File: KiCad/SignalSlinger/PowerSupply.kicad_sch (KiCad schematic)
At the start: 44 parts, among them J201 Barrel_Jack_Switch, J203 External Fan Power, J204 Controlled Power, U201 LP2985-3.3, U202 LP2985-3.3, U203 TPS63060, U204 TPS22810DBVT, U205 uA7805

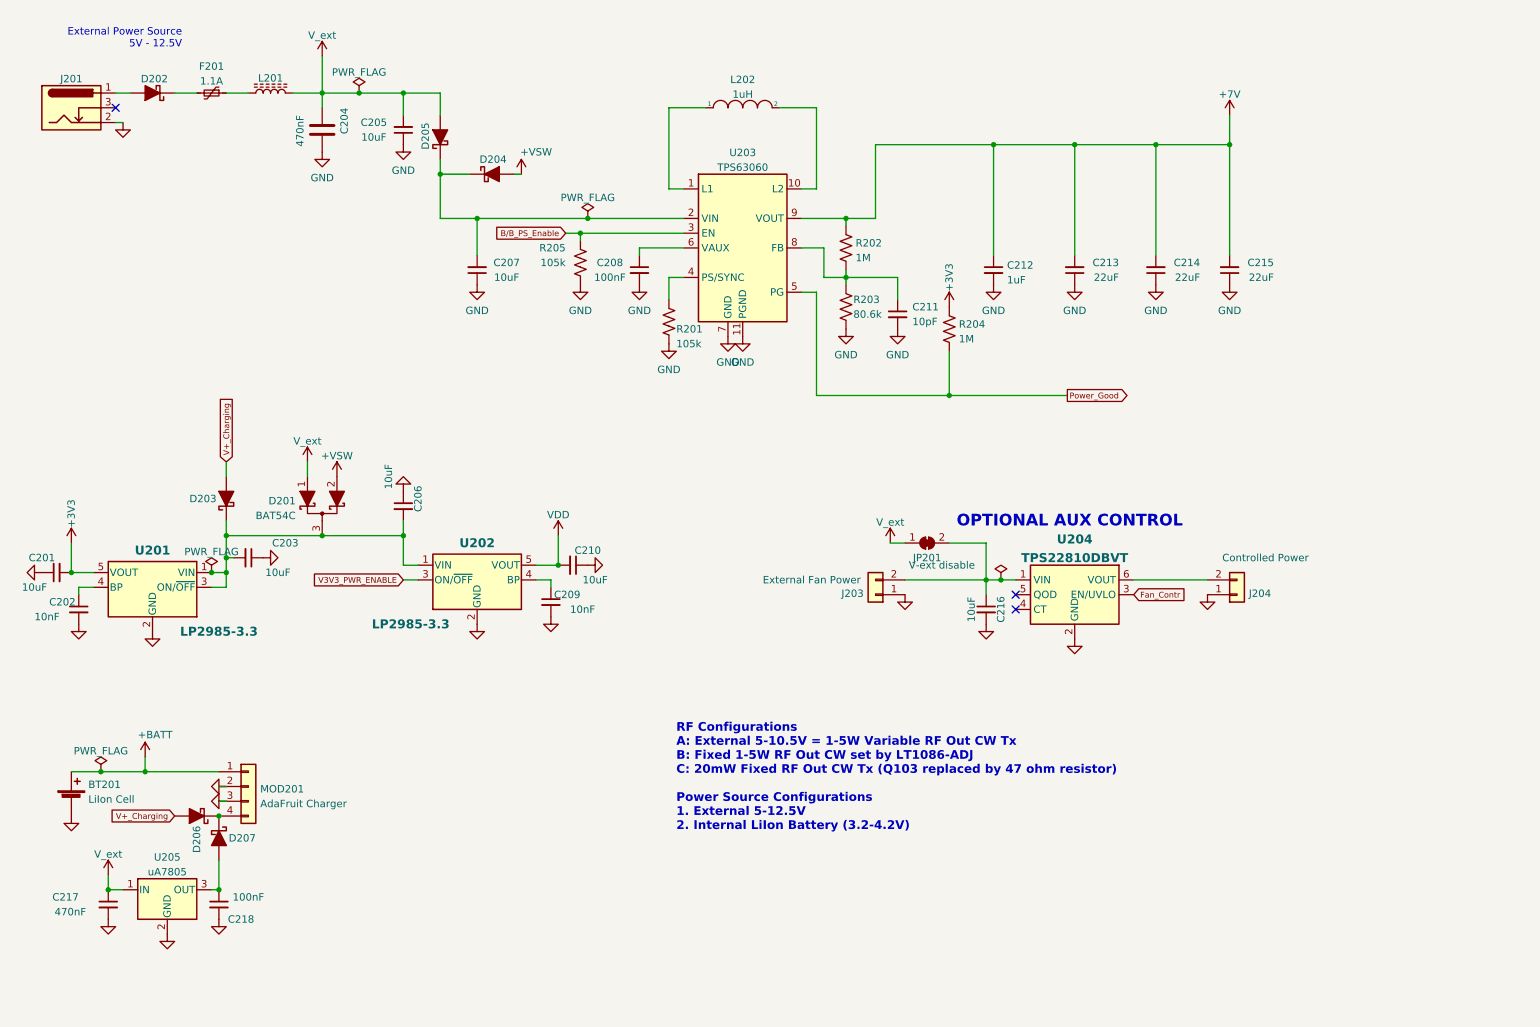
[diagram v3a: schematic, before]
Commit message: Added voltage divider
Now supports monitoring external battery voltage.
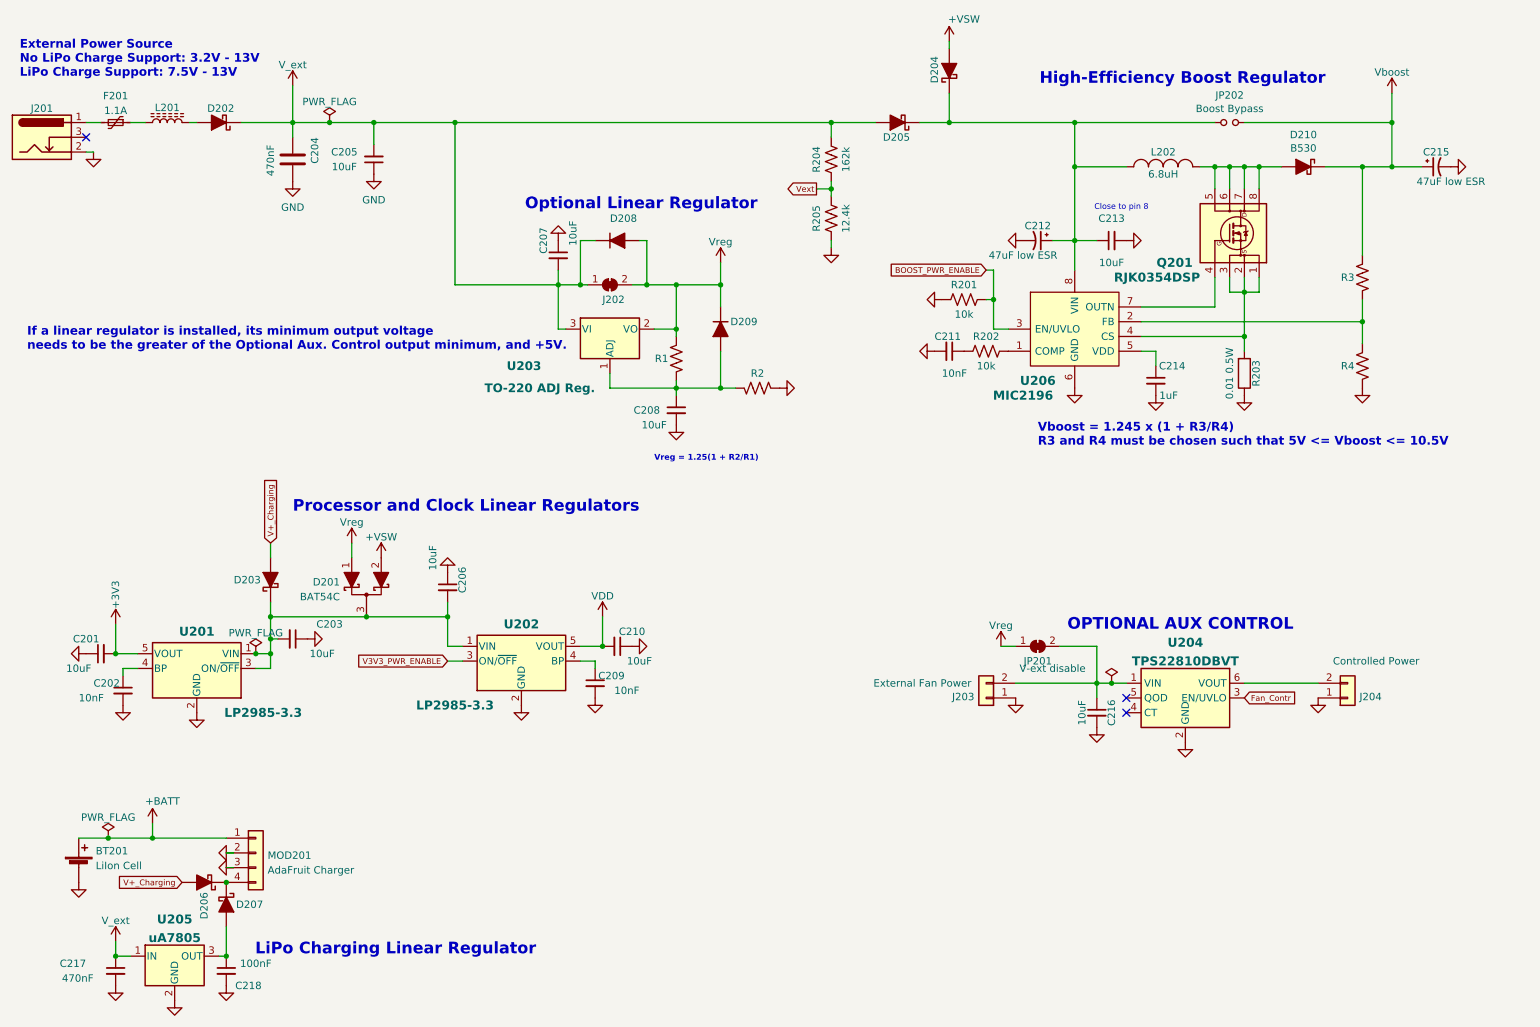
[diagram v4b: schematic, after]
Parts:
- removed C212: 1uF, Capacitor_SMD:C_0805_2012Metric, symbol Device:C_Small
- removed C215: 22uF, Capacitor_SMD:C_0805_2012Metric, symbol Device:C_Small
- removed L202: 1uH, Inductor_SMD:L_Bourns_SRN5040TA, symbol pspice:INDUCTOR
- removed R203: 80.6k, Resistor_SMD:R_0805_2012Metric, symbol Device:R_Small_US
- removed U203: TPS63060, Package_SON:Texas_S-PWSON-N10_ThermalVias, symbol Regulator_Switching:TPS63060
- added C212, C215: 47uF low ESR, Capacitors:C_2917, symbol Device:CP1_Small-Device
- added D208, D209: 1N4001, Diode_SMD:D_SOD-123F, symbol Diode:1N914WT
- added D210: B530, Diode_SMD:D_SMC, symbol FlexFox80-rescue:D_Schottky_ALT-Device
- added J202: SolderJumper_2_Bridged, Jumper:SolderJumper-2_P1.3mm_Bridged_RoundedPad1.0x1.5mm, symbol Jumper:SolderJumper_2_Bridged
- added JP202: Boost Bypass, Jumper:SolderJumper-2_P1.3mm_Open_RoundedPad1.0x1.5mm, symbol FlexFox80-rescue:Jumper_NO_Small-Device
- added L202: 6.8uH, Inductors:CDR7D28MN, symbol FlexFox80-rescue:INDUCTOR_SMALL-ARDF-2-Band-MiniTx-rescue
- added Q201: RJK0354DSP, Package_SO:SOIC-8_3.9x4.9mm_P1.27mm, symbol FlexFox80-rescue:SI4884BDY-Transistor_FET
- added R1, R2, R3, R4: TBD, Resistor_THT:R_Axial_DIN0204_L3.6mm_D1.6mm_P2.54mm_Vertical, symbol Device:R_Small_US
- added R203: 0.01 0.5W, Resistor_SMD:R_0805_2012Metric, symbol Device:R
- added U203: TO-220 ADJ Reg., Package_TO_SOT_THT:TO-220-3_Horizontal_TabDown, symbol Regulator_Linear:LT1086-ADJ
- added U206: MIC2196, Package_SO:SOIC-8_3.9x4.9mm_P1.27mm, symbol FlexFox80-rescue:MIC2196-Power_Management
- C208: value 100nF -> 10uF; Digi-Key Part No. 1276-1099-1-ND -> 445-14418-1-ND; LCSC Part Number C29926 -> C3843628; Link https://www.digikey.com/short/q2f22qnq -> https://www.digikey.com/short/p8qdn4mp; Manufacturer Samsung Electro-Mechanics -> TDK Corporation; Manufacturer PN CL21B104KACNNNC -> C2012X5R1V106K125AC
- C211: value 10pF -> 10nF; Digi-Key Part No. 478-KGM21BCG1H100JTCT-ND -> 399-C0805C103J5GEC7800CT-ND; LCSC Part Number C157608 -> C3887673; Link https://www.digikey.com/en/products/detail/kyocera-avx/KGM2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 -> https://www.digikey.com/short/qd893213; Manufacturer KYOCERA AVX -> KEMET; Manufacturer PN KGM21BCG1H100JT -> C0805C103J5GEC7800
- C213: value 22uF -> 10uF; Digi-Key Part No. 1276-6780-1-ND -> 445-14418-1-ND; LCSC Part Number (none) -> C3843628; Link (none) -> https://www.digikey.com/short/p8qdn4mp; Manufacturer Samsung Electro-Mechanics -> TDK Corporation; Manufacturer PN CL21A226MOCLRNC -> C2012X5R1V106K125AC
- C214: value 22uF -> 1uF; Digi-Key Part No. 1276-6780-1-ND -> 311-1365-1-ND; LCSC Part Number (none) -> C344171; Link (none) -> <a href="https://www.digikey.com/products/en?keywords=311-1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; Manufacturer Samsung Electro-Mechanics -> Yageo; Manufacturer PN CL21A226MOCLRNC -> CC0805KKX7R7BB105
- R201: value 105k -> 10k; footprint Resistor_SMD:R_0805_2012Metric -> Capacitor_SMD:C_0805_2012Metric; Digi-Key Part No. 311-105KCRCT-ND -> RNCP0805FTD10K0CT-ND; LCSC Part Number C273877 -> C2441435; Link https://www.digikey.com/en/products/detail/yageo/RC0805FR-0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 -> https://www.digikey.com/en/products/detail/stackpole-electr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; Manufacturer YAGEO -> Stackpole Electronics Inc; Manufacturer PN RC0805FR-07105KL -> RNCP0805FTD10K0
- R202: value 1M -> 10k; footprint Resistor_SMD:R_0805_2012Metric -> Capacitor_SMD:C_0805_2012Metric; Digi-Key Part No. 13-RC0805FR-131MLCT-ND -> RNCP0805FTD10K0CT-ND; LCSC Part Number C4198744 -> C2441435; Link https://www.digikey.com/en/products/detail/yageo/RC0805FR-1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 -> https://www.digikey.com/en/products/detail/stackpole-electr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; Manufacturer YAGEO -> Stackpole Electronics Inc; Manufacturer PN RC0805FR-131ML -> RNCP0805FTD10K0
- R204: value 1M -> 162k; Digi-Key Part No. 13-RC0805FR-131MLCT-ND -> 311-162KCRCT-ND; LCSC Part Number C4198744 -> C273888; Link https://www.digikey.com/en/products/detail/yageo/RC0805FR-1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 -> https://www.digikey.com/en/products/detail/yageo/RC0805FR-0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; Manufacturer PN RC0805FR-131ML -> RC0805FR-07162KL
- R205: value 105k -> 12.4k; Digi-Key Part No. 311-105KCRCT-ND -> 311-12.4KCRCT-ND; LCSC Part Number C273877 -> C137595; Link https://www.digikey.com/en/products/detail/yageo/RC0805FR-07105KL/727548 -> https://www.digikey.com/en/products/detail/yageo/RC0805FR-0712K4L/727572; Manufacturer PN RC0805FR-07105KL -> RC0805FR-0712K4L
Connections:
- net Power_Good is gone; now on net V_ext: R204.2
- net +3V3: no longer R204.1
- net GND: now also C213.2, C214.2, R201.1, C212.2, C215.2, R2.1, R203.1, R4.1, U206.6 (GND); no longer C213.1, C214.1, R201.2
- net V_ext: now also C207.2, D202.1 (K), D208.1 (K), J202.1 (A), U203.3 (VI); no longer D201.1 (K), JP201.1 (A), L201.2
- net at C211.1: now also R202.1; no longer R202.2
- net at F201.2: now also J201.1; no longer D202.1 (K)
- net at D204.1 (K), D205.1 (K): now also C213.1, C212.1, JP202.2, L202.2, U206.8 (VIN); no longer C207.2
- net at D202.2 (A): now also L201.2; no longer J201.1
- net at C208.1: now also D209.2 (A), R1.1, R2.2, U203.1 (ADJ)
- removed net +7V: C213.2, C214.2, R202.1
- net B/B_PS_Enable renamed Vext
- net Vext: now also R204.1
- new net: Q201.1 (S), Q201.2 (S), Q201.3 (S), R203.2, U206.4 (CS)
- new net: Q201.4 (G), U206.7 (OUTN)
- new net: D210.2 (A), L202.1, Q201.5 (D), Q201.6 (D), Q201.7 (D), Q201.8 (D)
- new net: C214.1, U206.5 (VDD)
- new net: R3.1, R4.2, U206.2 (FB)
- new net: R202.2, U206.1 (COMP)
- new net BOOST_PWR_ENABLE: R201.2, U206.3 (EN/UVLO)
- new net Vdrive: C215.1, D201.1 (K), D208.2 (A), D209.1 (K), D210.1 (K), J202.2 (B), JP201.1 (A), JP202.1, R1.2, R3.2, U203.2 (VO)
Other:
- note added: "Close to pin 8"
- note added: "External Power Source No LiPo Charge Support: 3.2V - 13V LiPo Charge Support: 7.5V - 13V"
- note added: "High-Efficiency Boost Regulator"
- note added: "If a linear regulator is installed, its minimum output voltage needs to be the greater of the Optional Aux. Control output minimum, and +5V."
- note added: "LiPo Charging Linear Regulator"
- note added: "Optional Linear Regulator"
- note added: "Processor and Clock Linear Regulators"
- note added: "Vboost = 1.245 x (1 + R3/R4) R3 and R4 must be chosen such that 5V <= Vboost <= 10.5V"
- note added: "Vreg = 1.25(1 + R2/R1)"
- note removed: "External Power Source 5V - 12.5V"
- note removed: "RF Configurations A: External 5-10.5V = 1-5W Variable RF Out CW Tx B: Fixed 1-5W RF Out CW set by LT1086-ADJ C: 20mW Fixed RF Out CW Tx (Q103 replaced by 47 ohm resistor) Power Source Configurations 1. External 5-12.5V 2. Internal LiIon Battery (3.2-4.2V)"
- moved on the sheet: BT201, C201, C202, C203, C204, C205, C206, C209, C210, C216, C217, C218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

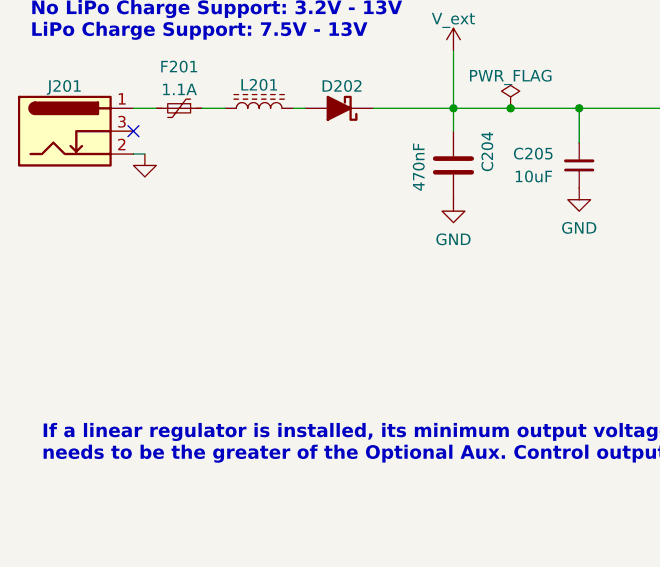
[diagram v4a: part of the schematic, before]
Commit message: Comment updates
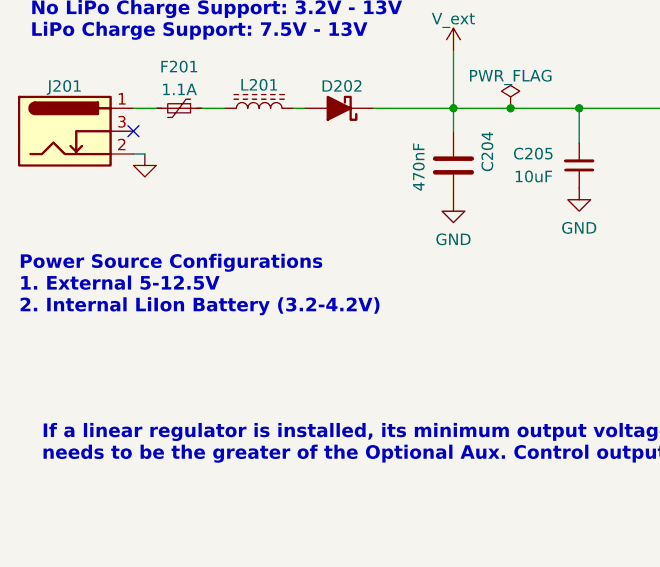
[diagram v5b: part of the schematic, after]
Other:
- note added: "Power Source Configurations 1. External 5-12.5V 2. Internal LiIon Battery (3.2-4.2V)"
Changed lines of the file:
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@@
     (effects (font (size 1 1) (thickness 0.2) bold) (justify left bottom))
+  )
+  (text "Power Source Configurations\n1. External 5-12.5V\n2. Internal LiIon Battery (3.2-4.2V)\n\n"
+    (at 20.32 63.5 0)
+    (effects (font (size 1.5 1.5) (thickness 0.3) bold) (justify left bottom))
   )
   (global_label "V3V3_PWR_ENABLE" (shape input) (at 95.25 130.81 180) (fields_autoplaced)

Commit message: Extensive Cleanup
BOM scrub
Added jumpers for foxoring power level
PCB ground plane improvements
Updated Gerbers
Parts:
- R201, R202: footprint Capacitor_SMD:C_0805_2012Metric -> Resistor_SMD:R_0805_2012Metric
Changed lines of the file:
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@@
     (property "Reference" "R201" (id 0) (at 184.15 66.04 90))
     (property "Value" "10k" (id 1) (at 184.15 71.12 90))
-    (property "Footprint" "Capacitor_SMD:C_0805_2012Metric" (id 2) (at 184.15 68.58 0)
+    (property "Footprint" "Resistor_SMD:R_0805_2012Metric" (id 2) (at 184.15 68.58 0)
       (effects (font (size 1.27 1.27)) hide)
     )
@@
     (property "Reference" "R202" (id 0) (at 187.96 74.93 90))
     (property "Value" "10k" (id 1) (at 187.96 80.01 90))
-    (property "Footprint" "Capacitor_SMD:C_0805_2012Metric" (id 2) (at 187.96 77.47 0)
-      (effects (font (size 1.27 1.27)) hide)
-    )
+    (property "Footprint" "Resistor_SMD:R_0805_2012Metric" (id 2) (at 187.96 77.47 0)
+      (effects (font (size 1.27 1.27)) hide)
+    )
